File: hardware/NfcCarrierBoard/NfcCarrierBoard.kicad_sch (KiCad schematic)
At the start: 3 parts

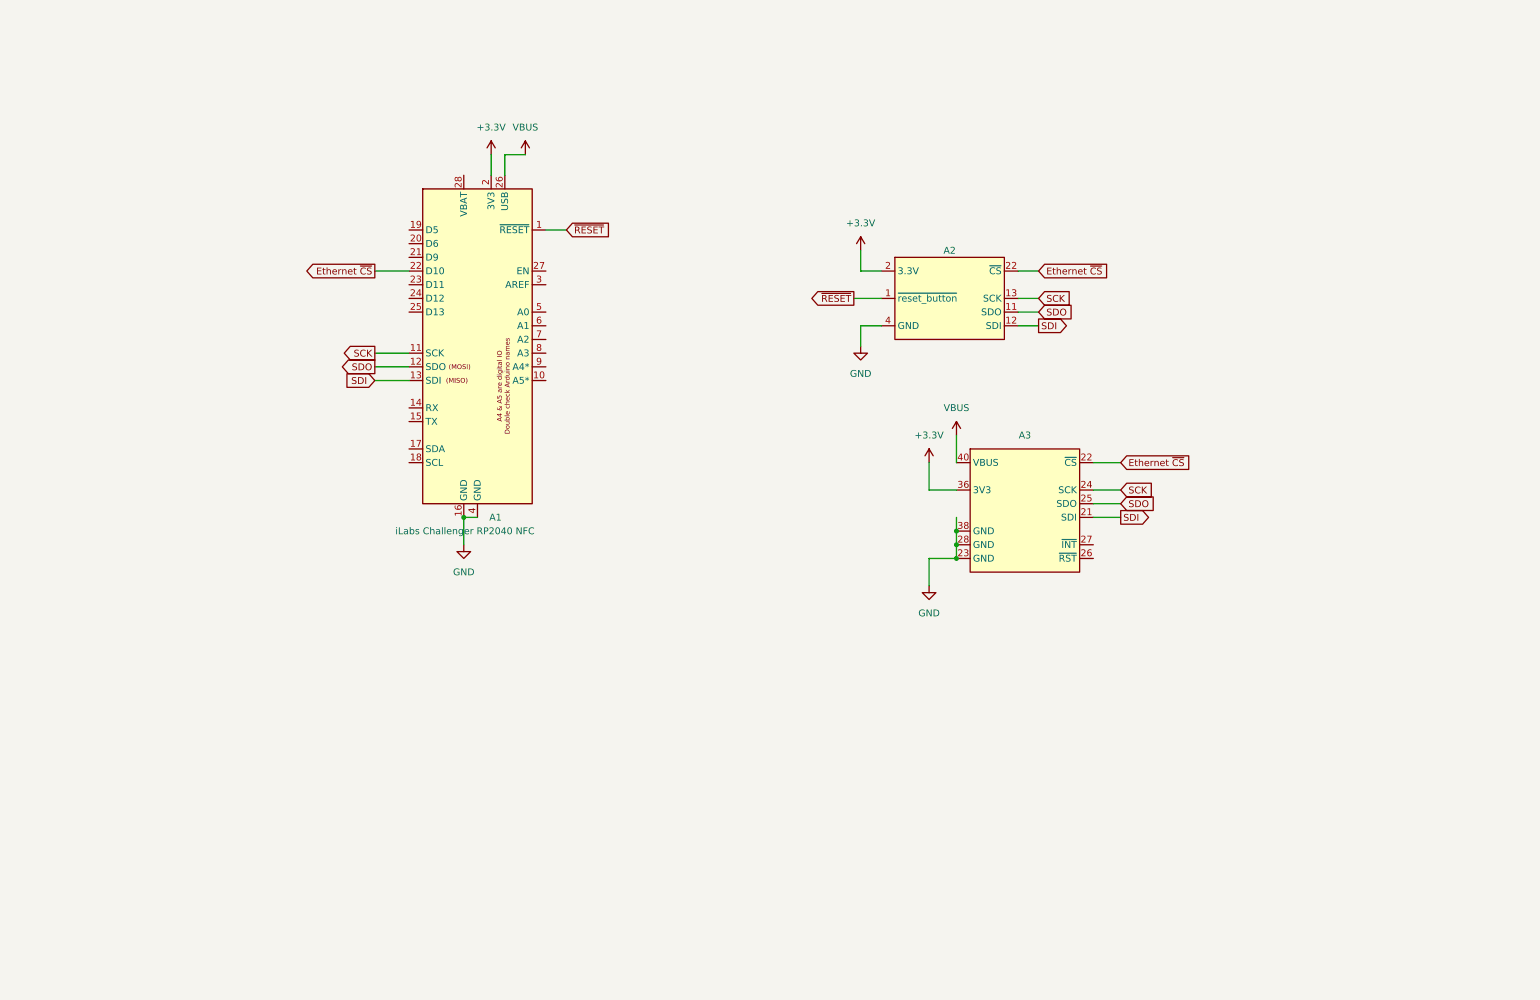
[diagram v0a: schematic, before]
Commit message: Lots of schematic changes that should have been commited incrementally.
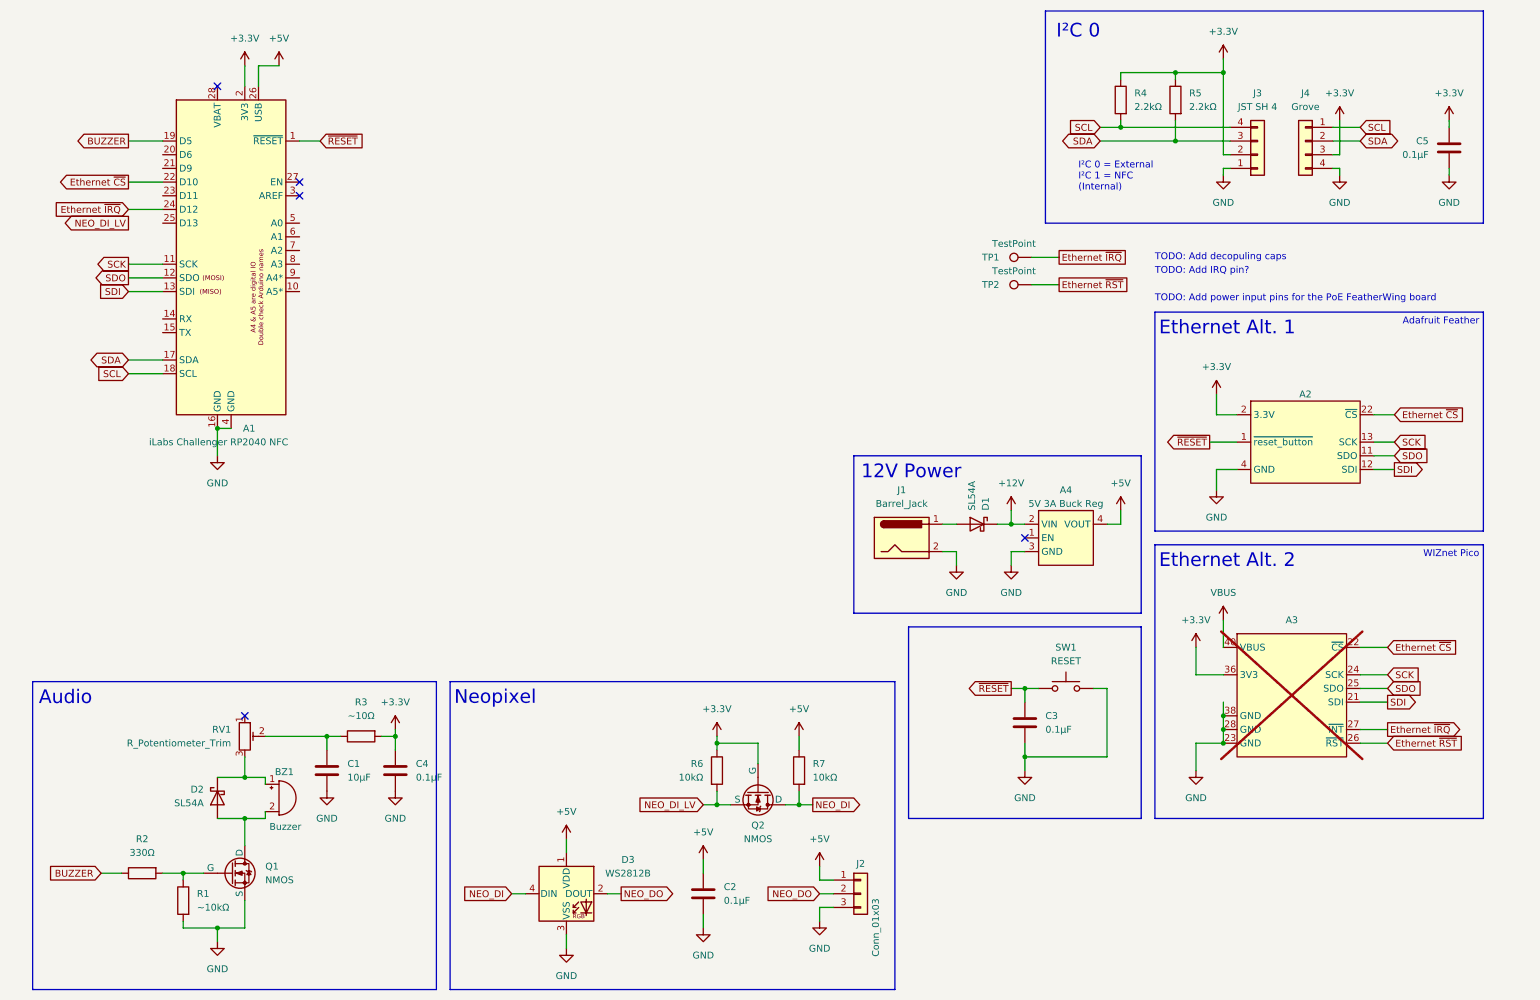
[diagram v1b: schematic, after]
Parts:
- added A4: 5V 3A Buck Reg, FootprintLibrary:SparkFun BabyBuck Regulator 5V, symbol SymbolLibrary:SparkFun_BabyBuck_Regulator_Breakout
- added BZ1: Buzzer, symbol Device:Buzzer
- added C1: 10µF, Capacitor_SMD:C_0805_2012Metric_Pad1.18x1.45mm_HandSolder, symbol Device:C
- added C2, C3, C4, C5: 0.1µF, Capacitor_SMD:C_0805_2012Metric_Pad1.18x1.45mm_HandSolder, symbol Device:C
- added D1, D2: SL54A, Diode_SMD:D_SMA-SMB_Universal_Handsoldering, symbol Device:D_Schottky
- added D3: WS2812B, LED_SMD:LED_WS2812B_PLCC4_5.0x5.0mm_P3.2mm, symbol LED:WS2812B
- added J1: Barrel_Jack, Connector_BarrelJack:BarrelJack_Horizontal, symbol Connector:Barrel_Jack
- added J2: Conn_01x03, Connector_PinHeader_2.54mm:PinHeader_1x03_P2.54mm_Vertical, symbol Connector_Generic:Conn_01x03
- added J3: JST SH 4, symbol Connector_Generic:Conn_01x04
- added J4: Grove, Connector:NS-Tech_Grove_1x04_P2mm_Vertical, symbol Connector_Generic:Conn_01x04
- added Q1, Q2: NMOS, symbol Simulation_SPICE:NMOS
- added R1: ~10kΩ, Resistor_SMD:R_0805_2012Metric_Pad1.20x1.40mm_HandSolder, symbol Device:R
- added R2: 330Ω, Resistor_SMD:R_0805_2012Metric_Pad1.20x1.40mm_HandSolder, symbol Device:R
- added R3: ~10Ω, Resistor_SMD:R_0805_2012Metric_Pad1.20x1.40mm_HandSolder, symbol Device:R
- added R4, R5: 2.2kΩ, Resistor_SMD:R_0805_2012Metric_Pad1.20x1.40mm_HandSolder, symbol Device:R
- added R6, R7: 10kΩ, Resistor_SMD:R_0805_2012Metric_Pad1.20x1.40mm_HandSolder, symbol Device:R
- added RV1: R_Potentiometer_Trim, Capacitor_SMD:C_0805_2012Metric_Pad1.18x1.45mm_HandSolder, symbol Device:R_Potentiometer_Trim
- added SW1: RESET, symbol Switch:SW_Push
- added TP1, TP2: TestPoint, symbol Connector:TestPoint
- A3: now not fitted; now left out of the parts list
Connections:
- net +3.3V: now also C4.1, C5.1, J3.2 (Pin_2), J4.3 (Pin_3), Q2.2 (G), R3.2, R4.1, R5.1, R6.1
- net GND: now also A4.3 (GND), C1.2, C2.2, C3.2, C4.2, C5.2, D3.3 (VSS), J1.2, J2.3 (Pin_3), J3.1 (Pin_1), J4.4 (Pin_4), Q1.3 (S), R1.2, SW1.2
- net VBUS: no longer A1.26 (USB)
- net ~{RESET}: now also C3.1, SW1.1
- net SDA: now reaches A1.17 (SDA)
- net SDA: now also J3.3 (Pin_3), J4.2 (Pin_2), R5.2
- net SCL: now reaches A1.18 (SCL)
- net SCL: now also J3.4 (Pin_4), J4.1 (Pin_1), R4.2
- net BUZZER: now reaches A1.19 (D5)
- net BUZZER: now also R2.1
- net Ethernet ~{IRQ}: now reaches A1.24 (D12)
- net Ethernet ~{IRQ}: now also A3.27 (~{INT}), TP1.1
- net Ethernet ~{RST}: now reaches A3.26 (~{RST})
- net Ethernet ~{RST}: now also TP2.1
- new net: Q1.2 (G), R1.1, R2.2
- new net: D1.2 (A), J1.1
- new net: BZ1.1 (+), D2.1 (K), RV1.3
- new net: BZ1.2 (-), D2.2 (A), Q1.1 (D)
- new net: C1.1, R3.1, RV1.2
- new net +12V: A4.2 (VIN), D1.1 (K)
- new net +5V: A1.26 (USB), A4.4 (VOUT), C2.1, D3.1 (VDD), J2.1 (Pin_1), R7.1
- new net NEO_DI: D3.4 (DIN), Q2.1 (D), R7.2
- new net NEO_DI_LV: Q2.3 (S), R6.2
- new net NEO_DO: D3.2 (DOUT), J2.2 (Pin_2)
- no-connect marks 0 -> 5
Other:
- note added: "12V Power"
- note added: "Adafruit Feather"
- note added: "Audio"
- note added: "Ethernet Alt. 1"
- note added: "Ethernet Alt. 2"
- note added: "I²C 0"
- note added: "Neopixel"
- note added: "TODO: Add IRQ pin?"
- note added: "TODO: Add decopuling caps"
- note added: "TODO: Add power input pins for the PoE FeatherWing board"
- note added: "WIZnet Pico"
- company: (none) -> EventAccess
- title: (none) -> NFC Carrier Board
- moved on the sheet: A1, A2

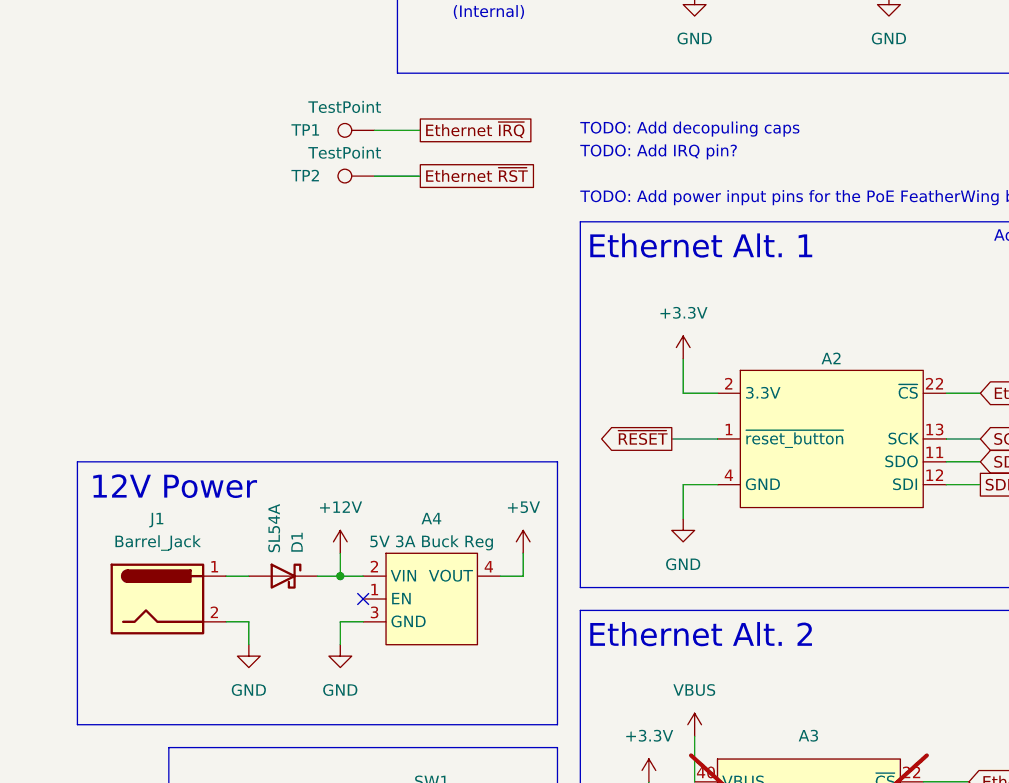
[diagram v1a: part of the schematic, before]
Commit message: Change 12V input symbol to jack with switch
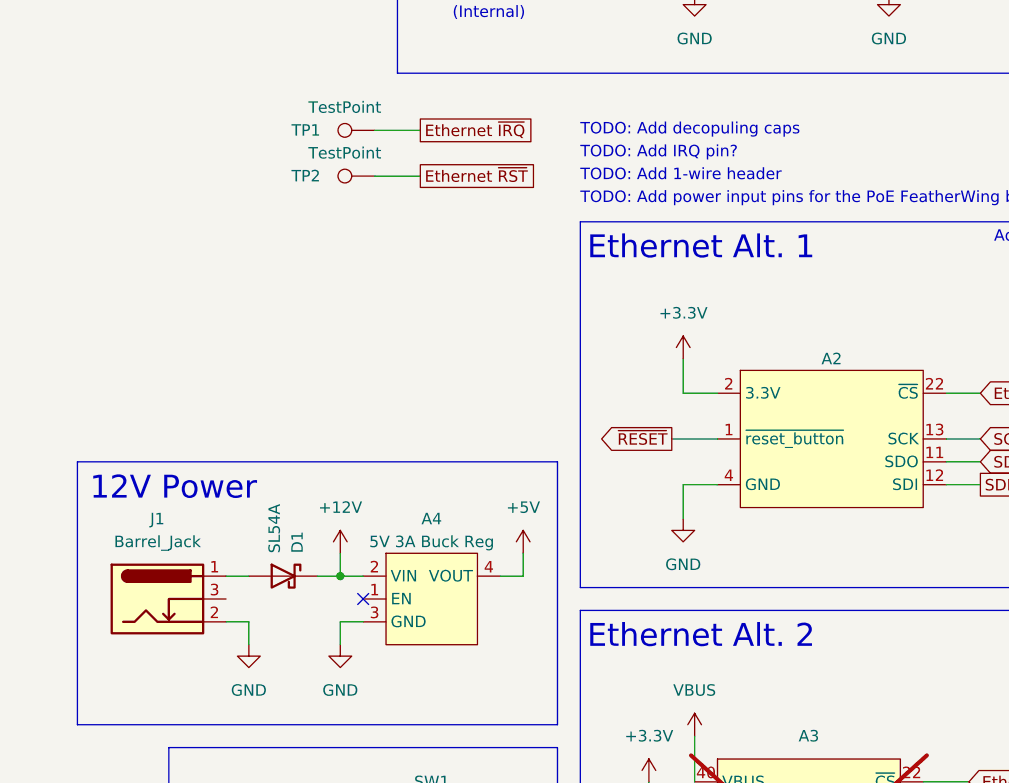
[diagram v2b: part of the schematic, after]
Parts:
- J1: symbol Connector:Barrel_Jack -> Connector:Barrel_Jack_Switch
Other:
- note added: "TODO: Add 1-wire header"
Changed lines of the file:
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@@
+		)
+	)
+	(text "TODO: Add 1-wire header"
+		(exclude_from_sim no)
+		(at 222.25 64.77 0)
+		(effects
+			(font
+				(size 1.27 1.27)
+			)
+			(justify left)
 		)
 	)
@@
 	)
 	(symbol
-		(lib_id "Connector:Barrel_Jack")
+		(lib_id "Connector:Barrel_Jack_Switch")
 		(at 175.26 111.76 0)
 		(unit 1)
@@
 			)
 		)
-		(property "Description" "DC Barrel Jack"
+		(property "Description" "DC Barrel Jack with an internal switch"
 			(at 175.26 111.76 0)
 			(effects
@@
 		(pin "2"
 		)
+		(pin "3"
+		)
 		(instances

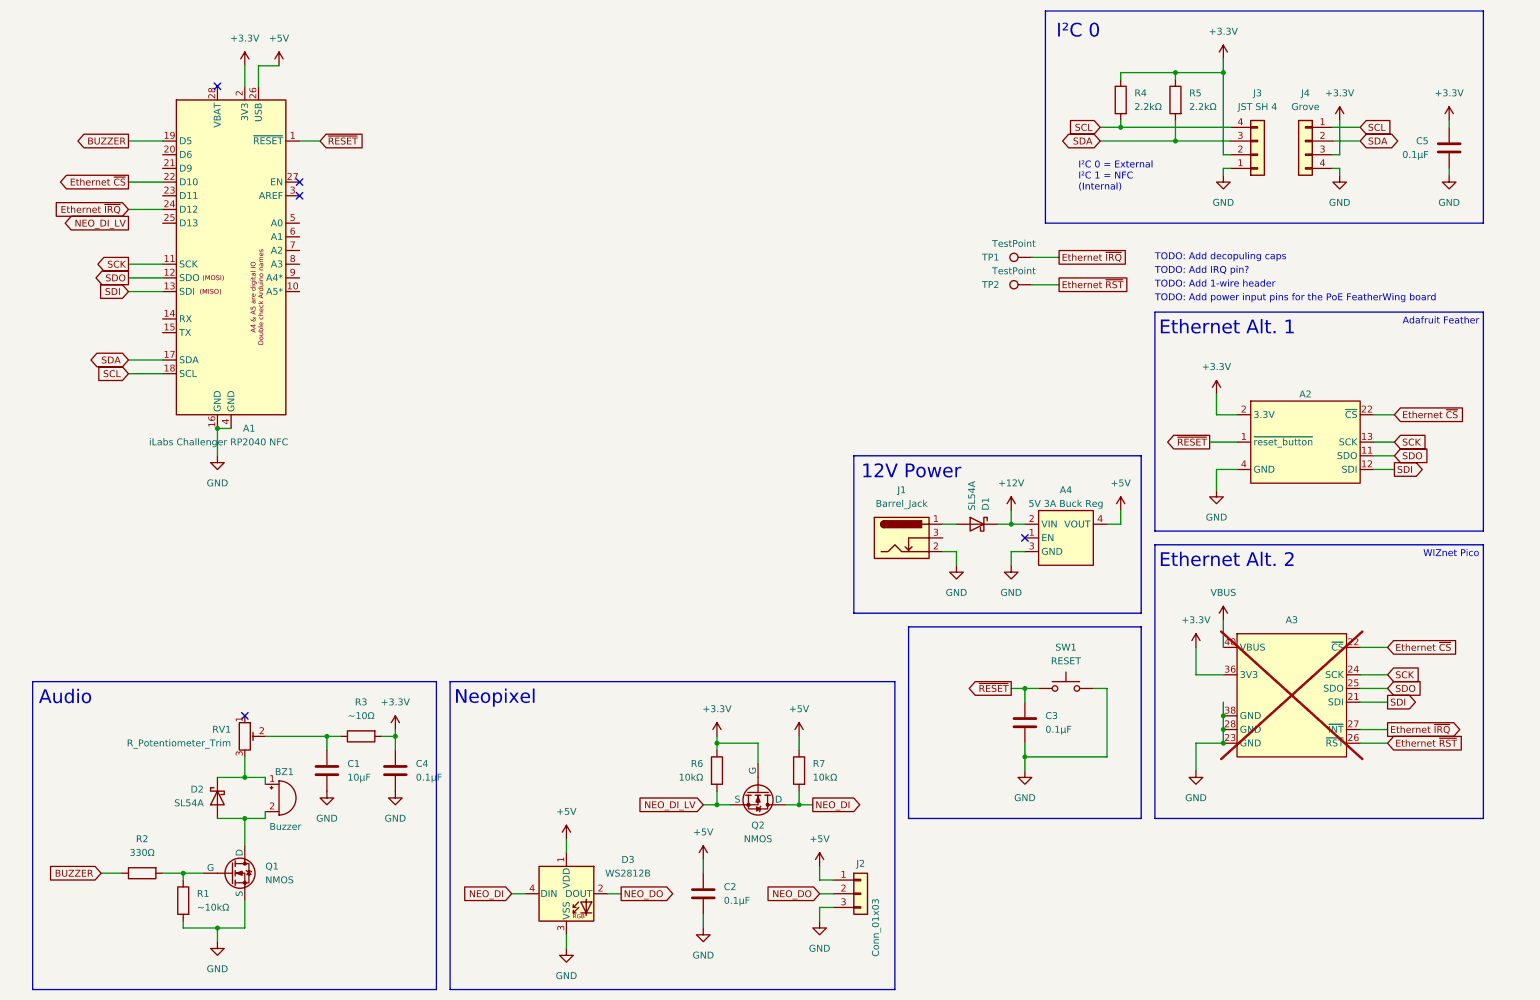
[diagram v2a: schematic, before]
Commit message: Add 1-Wire header
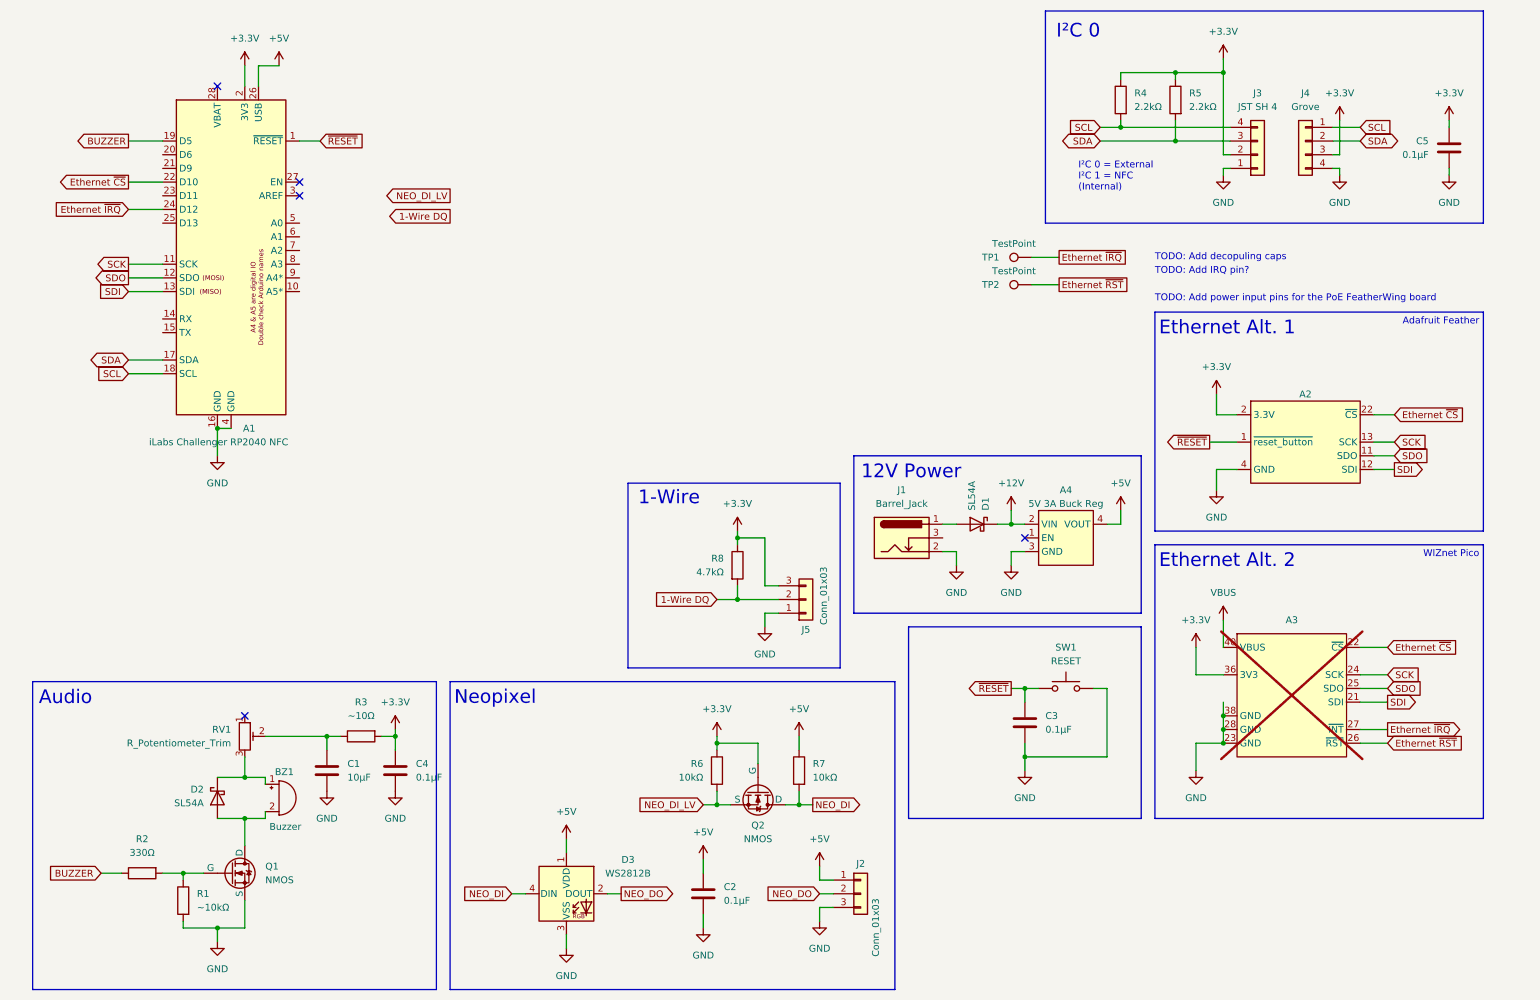
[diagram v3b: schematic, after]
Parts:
- added J5: Conn_01x03, Connector_PinHeader_2.54mm:PinHeader_1x03_P2.54mm_Vertical, symbol Connector_Generic:Conn_01x03
- added R8: 4.7kΩ, Resistor_SMD:R_0805_2012Metric_Pad1.20x1.40mm_HandSolder, symbol Device:R
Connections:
- net +3.3V: now also J5.3 (Pin_3), R8.1
- net GND: now also J5.1 (Pin_1)
- new net 1-Wire DQ: J5.2 (Pin_2), R8.2
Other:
- note added: "1-Wire"
- note removed: "TODO: Add 1-wire header"
